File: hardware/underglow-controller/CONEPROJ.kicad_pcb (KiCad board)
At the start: 4 copper layers, 86 x 97.7 mm, 141 parts, among them J2 U.FL-R-SMT-1(10), J3 DM3AT-SF-PEJM5, J4 DTM1312PA12PBR008, J5 Conn_01x10, J6 Conn_ARM_JTAG_SWD_10, J7 U.FL-R-SMT-1(10), Q2 Q_Dual_NMOS_S1G1S2G2D2D2D1D1, Q3 Q_Dual_NMOS_S1G1S2G2D2D2D1D1, Q4 Q_Dual_NMOS_S1G1S2G2D2D2D1D1, SW2 SW_Push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

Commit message: Add pullups to sdcard
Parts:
- added R40: 10k, Resistor_SMD:R_0402_1005Metric, F.Cu at (106.7, 114.6)
- added R43: 10k, Resistor_SMD:R_0402_1005Metric, F.Cu at (106.7, 113.5)
- added R44: 10k, Resistor_SMD:R_0402_1005Metric, F.Cu at (94.9, 119.8)
- added R45: 10k, Resistor_SMD:R_0402_1005Metric, F.Cu at (103.6, 119.8)
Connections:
- net /GPIO13 renamed /FSPICS2
- J3 pad 1: unconnected-(J3-Pad1) -> /SD_D2
- J3 pad 8: unconnected-(J3-Pad8) -> /SD_D1
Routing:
- net +3V3: track 528.9 -> 542.5 mm
- net /FSPID: track 218.7 -> 225.5 mm, vias 4 -> 5
- net /FSPIQ: track 220.4 -> 225.8 mm, vias 2 -> 4
- net /SD_D1: track 0.00 -> 3.09 mm
- net /SD_D2: track 0.00 -> 3.09 mm
- net GND: track 147.2 -> 148.1 mm, vias 80 -> 81

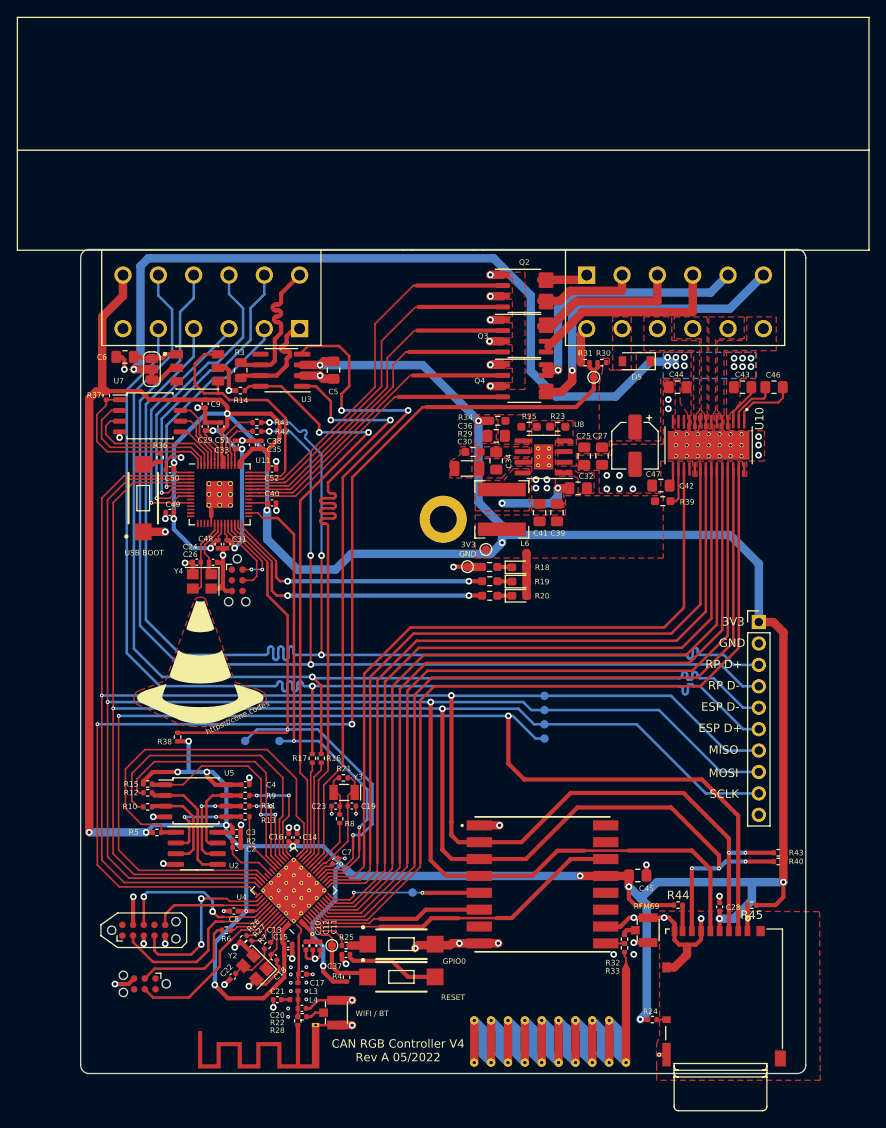
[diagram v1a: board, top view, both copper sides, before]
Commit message: Fix antenna impedance
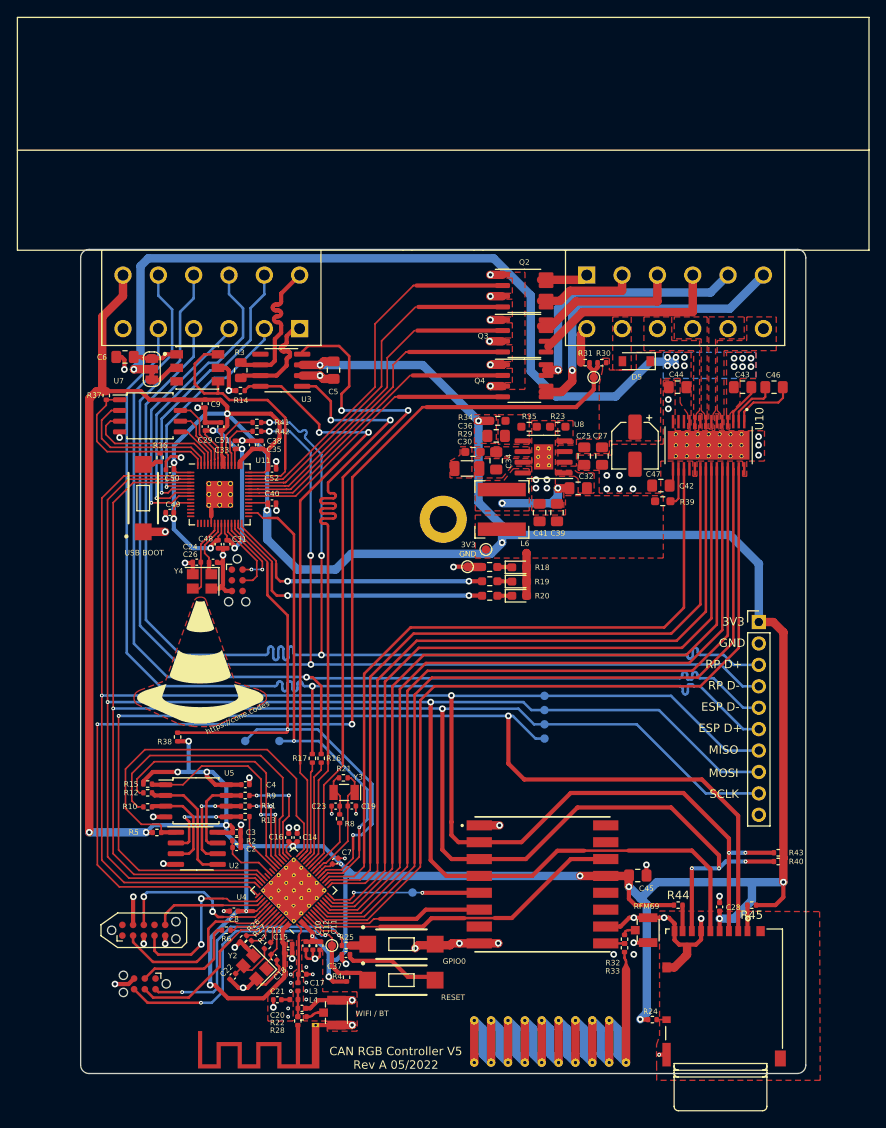
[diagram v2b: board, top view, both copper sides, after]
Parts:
- moved SW2 0.39 mm to (62.0, 128.7)
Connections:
- net Net-(AE3-Pad1) renamed /RF69_RF_ANT_PCB
- net Net-(J2-Pad2) renamed /RF69_RF_EXT
- net Net-(J7-Pad2) renamed /RF_ANT_EXT
- R25 pad 1: /GPIO0 -> /CTS
- TC2 pad 6: /RTS -> /CHIP_PU
- U4 pad 5: /GPIO0 -> /CTS
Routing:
- net /CTS: track 0.00 -> 34.8 mm, vias 0 -> 2
- net /CHIP_PU: track 11.4 -> 42.7 mm, vias 0 -> 2
- net /GPIO0: track 5.90 -> 0.00 mm
- net +3V3: track 542.5 -> 546.0 mm
- net GND: track 148.1 -> 150.0 mm, vias 81 -> 80
- net /GPIO1: track 38.9 -> 39.6 mm
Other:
- board text added: "CAN RGB Controller V5 Rev A 05/2022"
- board text removed: "CAN RGB Controller V4 Rev A 05/2022"

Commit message: add debug headers, change pmic to something in stock
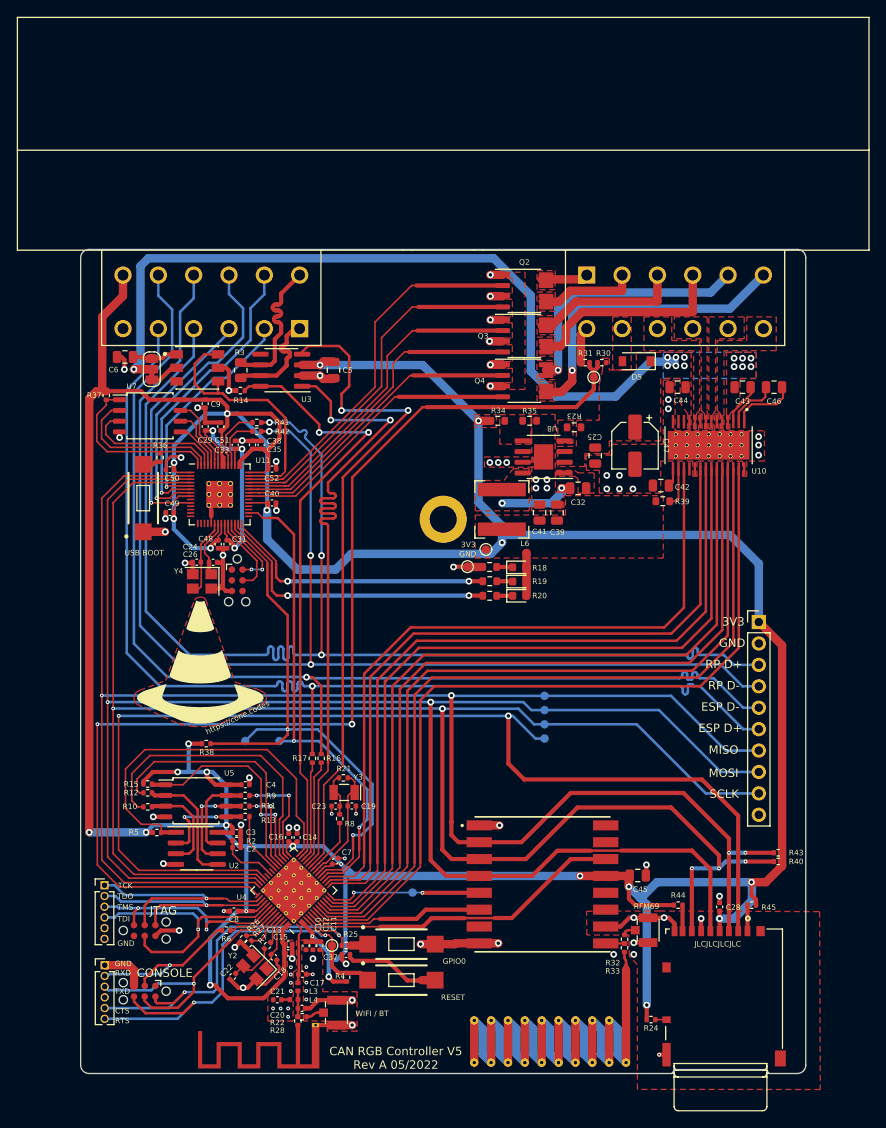
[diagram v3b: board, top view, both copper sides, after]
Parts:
- removed C27: 10uf, Capacitor_SMD:C_0805_2012Metric_Pad1.18x1.45mm_HandSolder
- removed C30: 5.6nf, Capacitor_SMD:C_1206_3216Metric
- removed C34, C36: DNP, Capacitor_SMD:C_0805_2012Metric_Pad1.18x1.45mm_HandSolder
- removed R29: 14k, Resistor_SMD:R_0603_1608Metric_Pad0.98x0.95mm_HandSolder
- added J8: JTAG, Connector_PinHeader_1.27mm:PinHeader_1x06_P1.27mm_Vertical, F.Cu at (26.8, 117.4)
- added TC4: TC2030-IDC, Connector:Tag-Connect_TC2030-IDC-NL_2x03_P1.27mm_Vertical, F.Cu at (31.6, 122.8)
- C25, C44: value 10uf -> 10uF; footprint Capacitor_SMD:C_0805_2012Metric_Pad1.18x1.45mm_HandSolder -> Capacitor_SMD:C_0805_2012Metric
- C32, C43: value 0.1uf -> 0.1uF; footprint Capacitor_SMD:C_0805_2012Metric_Pad1.18x1.45mm_HandSolder -> Capacitor_SMD:C_0805_2012Metric
- C39, C41: value DNP -> 22uF; footprint Capacitor_SMD:C_0805_2012Metric_Pad1.18x1.45mm_HandSolder -> Capacitor_SMD:C_0805_2012Metric
- C42: value 0.47uf -> 0.47uF; footprint Capacitor_SMD:C_0805_2012Metric_Pad1.18x1.45mm_HandSolder -> Capacitor_SMD:C_0805_2012Metric
- C45, C5, C6: footprint Capacitor_SMD:C_0805_2012Metric_Pad1.18x1.45mm_HandSolder -> Capacitor_SMD:C_0805_2012Metric
- C46: value 0.01uf -> 0.01uF; footprint Capacitor_SMD:C_0805_2012Metric_Pad1.18x1.45mm_HandSolder -> Capacitor_SMD:C_0805_2012Metric
- C47: value 10uf -> 10uF; footprint Capacitor_SMD:CP_Elec_5x5.9 -> Capacitor_SMD:CP_Elec_5x5.3
- D2, D3, D4: footprint LED_SMD:LED_0603_1608Metric_Pad1.05x0.95mm_HandSolder -> LED_SMD:LED_0603_1608Metric
- J6: value Conn_ARM_JTAG_SWD_10 -> CONSOLE; footprint Connector:Tag-Connect_TC2050-IDC-NL_2x05_P1.27mm_Vertical -> Connector_PinHeader_1.27mm:PinHeader_1x06_P1.27mm_Vertical
- R10, R11, R12, R13, R16, R17, R22, R28, R32, R33, R7, R8, R9: value 0 -> 0R
- R18, R19, R20: value 240 -> 240R; footprint Resistor_SMD:R_0603_1608Metric_Pad0.98x0.95mm_HandSolder -> Resistor_SMD:R_0603_1608Metric
- R23: value 200k -> 100k; footprint Resistor_SMD:R_0603_1608Metric_Pad0.98x0.95mm_HandSolder -> Resistor_SMD:R_0603_1608Metric
- R34: value 52.3k -> 31k6; footprint Resistor_SMD:R_0603_1608Metric_Pad0.98x0.95mm_HandSolder -> Resistor_SMD:R_0603_1608Metric
- R35: value 10k -> 10k2; footprint Resistor_SMD:R_0603_1608Metric_Pad0.98x0.95mm_HandSolder -> Resistor_SMD:R_0603_1608Metric
- R39: footprint Resistor_SMD:R_0603_1608Metric_Pad0.98x0.95mm_HandSolder -> Resistor_SMD:R_0603_1608Metric
- R6: value 499 -> 499R
- U8: value AP64200Q -> ADP2303ARDZ-3.3; footprint Package_SO:SOIC-8-1EP_3.9x4.9mm_P1.27mm_EP2.29x3mm_ThermalVias -> Package_SO:SOIC-8-1EP_3.9x4.9mm_P1.27mm_EP2.29x3mm
- moved J6 6.23 mm to (26.9, 126.9)
- moved R38 3.49 mm to (38.9, 100.6), turned to 0 degrees
- moved R23 1.93 mm to (82.5, 63.1)
- moved C25 1.30 mm to (85.0, 66.5)
- moved TC2 0.87 mm to (31.6, 130.0)
- moved R35 0.71 mm to (77.2, 62.3)
- moved R24 0.16 mm to (91.6, 133.3)
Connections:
- net Net-(C32-Pad1) renamed /BST
- net Net-(C32-Pad2) renamed /SW
- net Net-(C36-Pad2) renamed /FB
- J6 pad 1: unconnected-(J6-Pad1) -> GND
- J6 pad 2: /MTMS -> /RXD
- J6 pad 3: GND -> /TXD
- J6 pad 4: /MTCK -> unconnected-(J6-Pad4)
- J6 pad 5: GND -> /CTS
- J6 pad 6: /MTDO -> /CHIP_PU
- R23 pad 1: Net-(R23-Pad1) -> /VIN
- R23 pad 2: GND -> /PGOOD
- U8 pad 4: Net-(R23-Pad1) -> /PGOOD
- U8 pad 6: Net-(C34-Pad1) -> unconnected-(U8-Pad6)
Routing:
- net GND: track 150.0 -> 134.7 mm
- net /MTDO: track 13.5 -> 27.5 mm, vias 0 -> 1
- net /CHIP_PU: track 42.7 -> 55.1 mm
- net /TXD: track 21.0 -> 33.0 mm, vias 0 -> 1
- net /MTDI: track 20.9 -> 32.3 mm, vias 2 -> 1
- net /CTS: track 34.8 -> 46.1 mm
- net /MTCK: track 20.9 -> 29.5 mm, vias 2 -> 1
- net /RXD: track 13.3 -> 20.3 mm, vias 0 -> 1
- net +3V3: track 546.0 -> 540.5 mm
- net /GPIO14: track 73.7 -> 70.6 mm
- net /MTMS: track 22.3 -> 25.4 mm, vias 0 -> 2
- net /FSPICLK: track 215.4 -> 217.0 mm
- net /GPO4: track 23.2 -> 24.7 mm
- net Net-(C37-Pad1): track 11.4 -> 12.8 mm
- net /GPO1: track 5.66 -> 4.86 mm
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- added copper zone on F.Cu, net /GPO1
- added copper zone on F.Cu, net /GPO2
- added copper zone on F.Cu, net /GPO3
- added copper zone on F.Cu, net /GPO4
- added copper zone on F.Cu, net /GPO5
- added copper zone on F.Cu, net /GPO6
- added copper zone on F.Cu, net /PGOOD
- removed copper zone on F.Cu, net Net-(C30-Pad1)
- removed copper zone on F.Cu, net Net-(C34-Pad1)
- removed copper zone on F.Cu, net Net-(R23-Pad1)
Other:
- outline, holes or cut-outs redrawn
- board text added: "CONSOLE"
- board text added: "CTS"
- board text added: "JLCJLCJLCJLC"
- board text added: "JTAG"
- board text added: "RTS"
- board text added: "TCK"
- board text added: "TDI"
- board text added: "TDO"
- board text added: "TMS"

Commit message: misc cleanup
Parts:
- J2, J7: footprint U.FL-R-SMT-1_10_:HRS_U.FL-R-SMT-1(10) -> ConeCodes:HRS_U.FL-R-SMT-1(10)
- J3: footprint Connector_Hirose_SD:HRS_DM3AT-SF-PEJM5 -> ConeCodes:HRS_DM3AT-SF-PEJM5
- J4: footprint TE_DTM1312PA12PBR008:TE_DTM1312PA12PBR008 -> ConeCodes:TE_DTM1312PA12PBR008
- SW2, SW3, SW4: footprint SW_RS-032G05A3-SMRT:SW_RS-032G05A3-SMRT -> ConeCodes:SW_RS-032G05A3-SMRT
- U10: footprint DRV8844PWP:IC_TPS61196PWPRQ1 -> Package_SO:HTSSOP-28-1EP_4.4x9.7mm_P0.65mm_EP2.85x5.4mm_ThermalVias
- U11: footprint RP2040:RP2040-QFN-56 -> ConeCodes:QFN-56
- U4: footprint Package_DFN_QFN:QFN-56-1EP_7x7mm_P0.4mm_EP5.6x5.6mm_ThermalVias -> ConeCodes:QFN-56
- U6: footprint WS2815B:worldsemi-WS2815B-MFG -> ConeCodes:worldsemi-WS2815B-MFG
- U9: value RFM69HCW -> COM-13909; footprint XCVR_RFM69HW:XCVR_RFM69HW -> ConeCodes:XCVR_RFM69HW

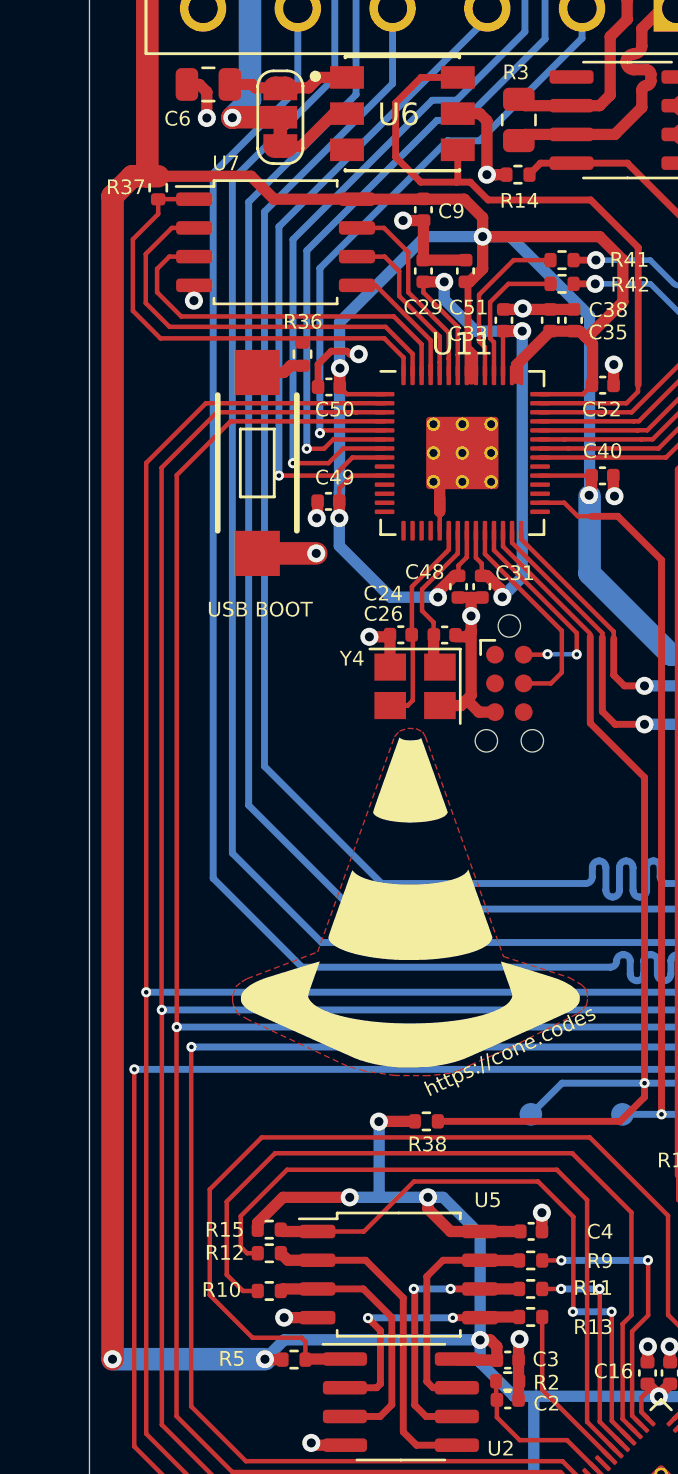
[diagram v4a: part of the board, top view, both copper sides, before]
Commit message: Update PCBs to share the same components
* 3x flash memory
* CAN transciever
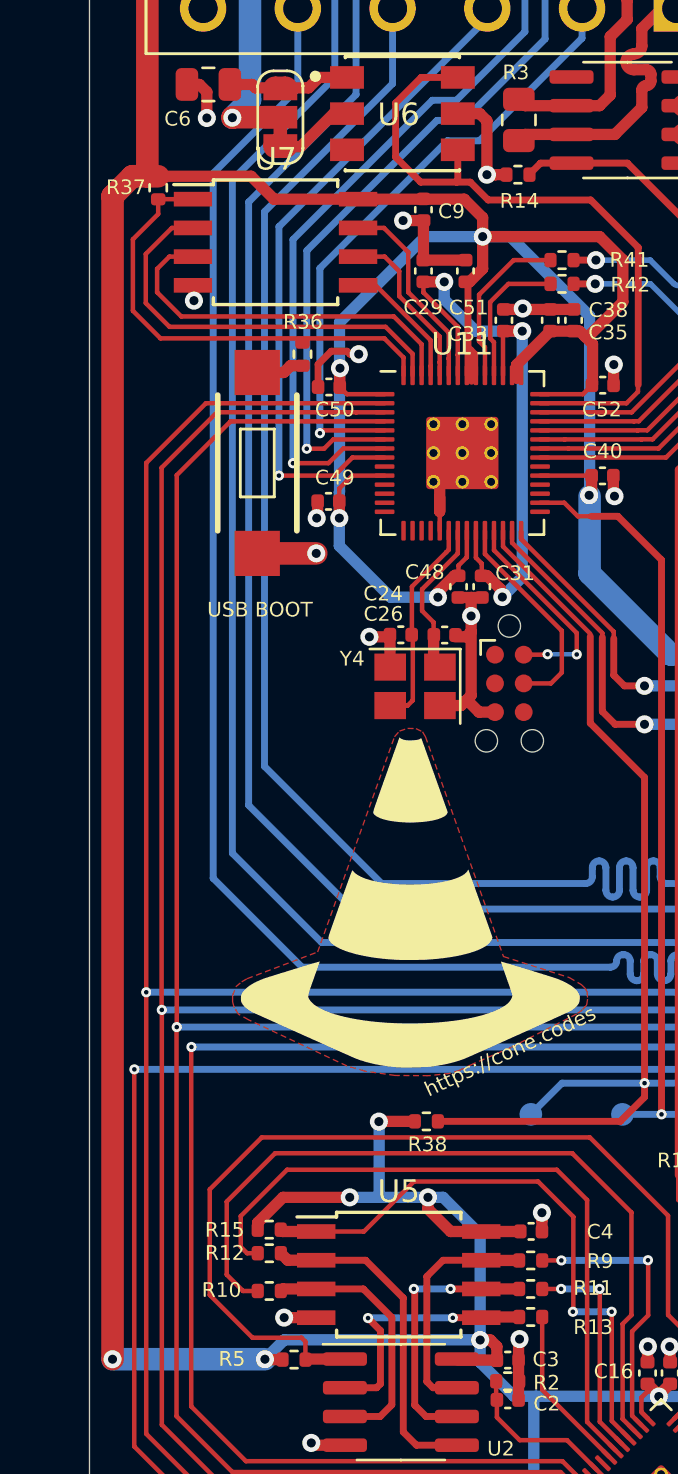
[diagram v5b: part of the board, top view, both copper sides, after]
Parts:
- U5, U7: footprint Package_SO:SOIC-8_5.23x5.23mm_P1.27mm -> Package_SO:SOIC-8W_5.3x5.3mm_P1.27mm
